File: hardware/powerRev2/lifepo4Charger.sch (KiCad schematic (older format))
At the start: 18 parts

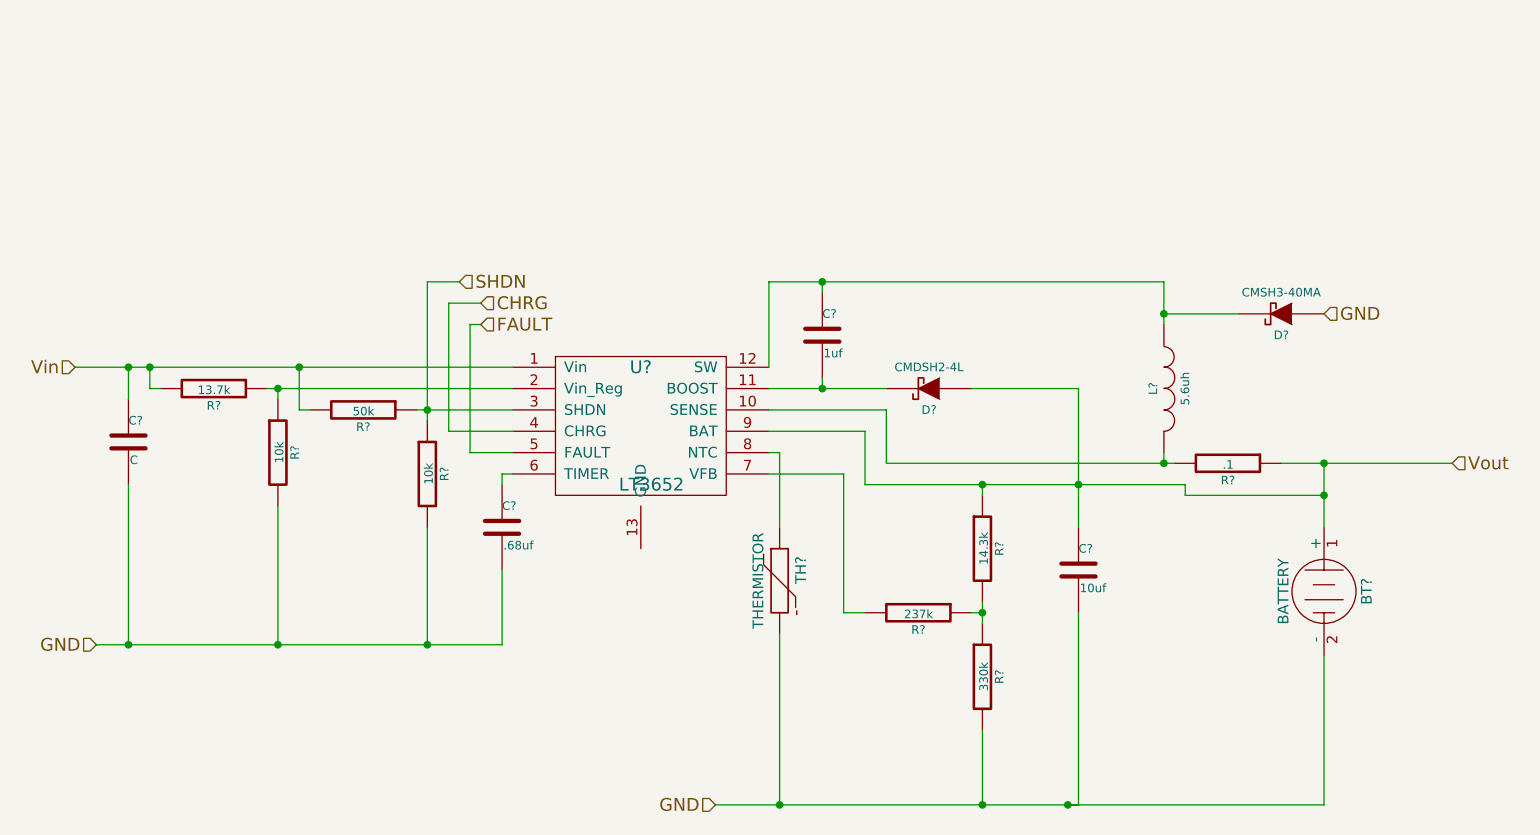
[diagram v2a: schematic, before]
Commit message: More work on the power supply
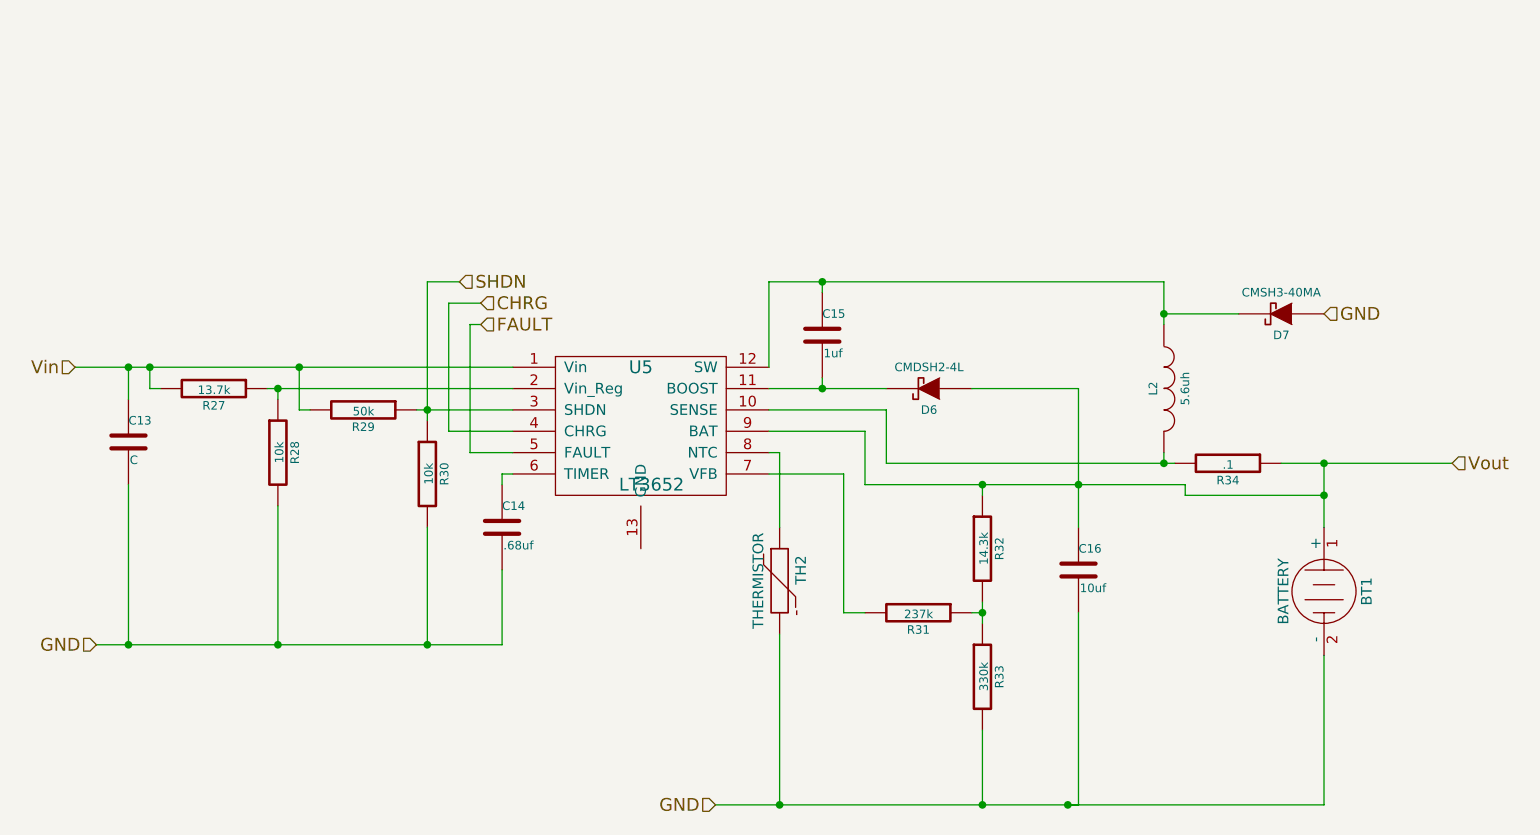
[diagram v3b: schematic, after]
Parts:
- gave numbers to parts that had none: 18
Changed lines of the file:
@@
 LIBS:KL03-QFN24
 LIBS:ncp508
+LIBS:hardwareRev1-cache
 LIBS:powerRev2-cache
 EELAYER 25 0
@@
 $EndDescr
 $Comp
-L LT3652 U?
+L LT3652 U5
 U 1 1 56114C94
 P 5850 3100
-F 0 "U?" H 5850 3400 60  0000 C CNN
+F 0 "U5" H 5850 3400 60  0000 C CNN
 F 1 "LT3652" H 5900 2850 60  0000 C CNN
 F 2 "" H 5850 2400 60  0000 C CNN
@@
 $EndComp
 $Comp
-L C C?
+L C C13
 U 1 1 56114CEB
 P 3450 3150
-F 0 "C?" H 3450 3250 40  0000 L CNN
+F 0 "C13" H 3450 3250 40  0000 L CNN
 F 1 "C" H 3456 3065 40  0000 L CNN
 F 2 "" H 3488 3000 30  0000 C CNN
@@
 $EndComp
 $Comp
-L R R?
+L R R27
 U 1 1 56114D05
 P 3850 2900
-F 0 "R?" V 3930 2900 40  0000 C CNN
+F 0 "R27" V 3930 2900 40  0000 C CNN
 F 1 "13.7k" V 3857 2901 40  0000 C CNN
 F 2 "" V 3780 2900 30  0000 C CNN
@@
 $EndComp
 $Comp
-L R R?
+L R R28
 U 1 1 56114DC8
 P 4150 3200
-F 0 "R?" V 4230 3200 40  0000 C CNN
+F 0 "R28" V 4230 3200 40  0000 C CNN
 F 1 "10k" V 4157 3201 40  0000 C CNN
 F 2 "" V 4080 3200 30  0000 C CNN
@@
 Vin
 $Comp
-L C C?
+L C C15
 U 1 1 56114F88
 P 6700 2650
-F 0 "C?" H 6700 2750 40  0000 L CNN
+F 0 "C15" H 6700 2750 40  0000 L CNN
 F 1 "1uf" H 6706 2565 40  0000 L CNN
 F 2 "" H 6738 2500 30  0000 C CNN
@@
 $EndComp
 $Comp
-L INDUCTOR L?
+L INDUCTOR L2
 U 1 1 56114FE2
 P 8300 2900
-F 0 "L?" V 8250 2900 40  0000 C CNN
+F 0 "L2" V 8250 2900 40  0000 C CNN
 F 1 "5.6uh" V 8400 2900 40  0000 C CNN
 F 2 "" H 8300 2900 60  0000 C CNN
@@
 $EndComp
 $Comp
-L DIODESCH D?
+L DIODESCH D7
 U 1 1 56115039
 P 8850 2550
-F 0 "D?" H 8850 2650 40  0000 C CNN
+F 0 "D7" H 8850 2650 40  0000 C CNN
 F 1 "CMSH3-40MA" H 8850 2450 40  0000 C CNN
 F 2 "" H 8850 2550 60  0000 C CNN
@@
 GND
 $Comp
-L C C?
+L C C16
 U 1 1 561153DF
 P 7900 3750
-F 0 "C?" H 7900 3850 40  0000 L CNN
+F 0 "C16" H 7900 3850 40  0000 L CNN
 F 1 "10uf" H 7906 3665 40  0000 L CNN
 F 2 "" H 7938 3600 30  0000 C CNN
@@
 $EndComp
 $Comp
-L BATTERY BT?
+L BATTERY BT1
 U 1 1 5611543C
 P 9050 3850
-F 0 "BT?" H 9050 4050 50  0000 C CNN
+F 0 "BT1" H 9050 4050 50  0000 C CNN
 F 1 "BATTERY" H 9050 3660 50  0000 C CNN
 F 2 "" H 9050 3850 60  0000 C CNN
@@
 	7900 2900 7900 3550
 $Comp
-L R R?
+L R R34
 U 1 1 56115725
 P 8600 3250
-F 0 "R?" V 8680 3250 40  0000 C CNN
+F 0 "R34" V 8680 3250 40  0000 C CNN
 F 1 ".1" V 8607 3251 40  0000 C CNN
 F 2 "" V 8530 3250 30  0000 C CNN
@@
 Connection ~ 9050 3400
 $Comp
-L THERMISTOR TH?
+L THERMISTOR TH2
 U 1 1 56115896
 P 6500 3800
-F 0 "TH?" V 6600 3850 50  0000 C CNN
+F 0 "TH2" V 6600 3850 50  0000 C CNN
 F 1 "THERMISTOR" V 6400 3800 50  0000 C CNN
 F 2 "" H 6500 3800 60  0000 C CNN
@@
 $EndComp
 $Comp
-L R R?
+L R R31
 U 1 1 561158DE
 P 7150 3950
-F 0 "R?" V 7230 3950 40  0000 C CNN
+F 0 "R31" V 7230 3950 40  0000 C CNN
 F 1 "237k" V 7157 3951 40  0000 C CNN
 F 2 "" V 7080 3950 30  0000 C CNN
@@
 $EndComp
 $Comp
-L R R?
+L R R32
 U 1 1 56115929
 P 7450 3650
-F 0 "R?" V 7530 3650 40  0000 C CNN
+F 0 "R32" V 7530 3650 40  0000 C CNN
 F 1 "14.3k" V 7457 3651 40  0000 C CNN
 F 2 "" V 7380 3650 30  0000 C CNN
@@
 $EndComp
 $Comp
-L R R?
+L R R33
 U 1 1 561159A8
 P 7450 4250
-F 0 "R?" V 7530 4250 40  0000 C CNN
+F 0 "R33" V 7530 4250 40  0000 C CNN
 F 1 "330k" V 7457 4251 40  0000 C CNN
 F 2 "" V 7380 4250 30  0000 C CNN
@@
 Connection ~ 4150 2900
 $Comp
-L R R?
+L R R29
 U 1 1 561165A5
 P 4550 3000
-F 0 "R?" V 4630 3000 40  0000 C CNN
+F 0 "R29" V 4630 3000 40  0000 C CNN
 F 1 "50k" V 4557 3001 40  0000 C CNN
 F 2 "" V 4480 3000 30  0000 C CNN
@@
 $EndComp
 $Comp
-L R R?
+L R R30
 U 1 1 561165FC
 P 4850 3300
-F 0 "R?" V 4930 3300 40  0000 C CNN
+F 0 "R30" V 4930 3300 40  0000 C CNN
 F 1 "10k" V 4857 3301 40  0000 C CNN
 F 2 "" V 4780 3300 30  0000 C CNN
@@
 FAULT
 $Comp
-L C C?
+L C C14
 U 1 1 56116AAD
 P 5200 3550
-F 0 "C?" H 5200 3650 40  0000 L CNN
+F 0 "C14" H 5200 3650 40  0000 L CNN
 F 1 ".68uf" H 5206 3465 40  0000 L CNN
 F 2 "" H 5238 3400 30  0000 C CNN
@@
 	5200 3300 5250 3300
 $Comp
-L DIODESCH D?
+L DIODESCH D6
 U 1 1 56116E89
 P 7200 2900
-F 0 "D?" H 7200 3000 40  0000 C CNN
+F 0 "D6" H 7200 3000 40  0000 C CNN
 F 1 "CMDSH2-4L" H 7200 2800 40  0000 C CNN
 F 2 "" H 7200 2900 60  0000 C CNN

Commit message: Started the new power board PCB. Made it pretty far.
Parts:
- C13: value C -> 10uf; footprint (none) -> Capacitors_SMD:C_0805
- C14: footprint (none) -> Capacitors_SMD:C_0402; Manufacturer PN (none) -> CL21F684ZAFNNNE
- C15: footprint (none) -> Capacitors_SMD:C_0402
- C16: footprint (none) -> Capacitors_SMD:C_0805
- D6: footprint (none) -> Diodes_SMD:SOD-323
- D7: footprint (none) -> Diodes_SMD:Diode-SMA_Standard
- L2: footprint (none) -> ASPI-6045S-5R6M-T:ASPI-6045S-5R6M-T; Manufacturer PN (none) -> ASPI-6045S-5R6M-T
- R27, R28, R29, R30, R31, R32, R33: footprint (none) -> Resistors_SMD:R_0402
- R34: footprint (none) -> Resistors_SMD:R_0805
- TH2: footprint (none) -> Pin_Headers:Pin_Header_Straight_1x02
- U6: renamed from U5; footprint (none) -> Housings_DFN_QFN:DFN-12-1EP_3x3mm_Pitch0.45mm
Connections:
- net GND: now also U6.13 (GND)
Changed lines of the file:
@@
 LIBS:ncp508
 LIBS:hardwareRev1-cache
+LIBS:Tag-Connect
+LIBS:mpcie
+LIBS:RF-Head2
+LIBS:ritli-rfhead
 LIBS:powerRev2-cache
 EELAYER 25 0
@@
 $EndDescr
 $Comp
-L LT3652 U5
+L LT3652 U6
 U 1 1 56114C94
 P 5850 3100
-F 0 "U5" H 5850 3400 60  0000 C CNN
+F 0 "U6" H 5850 3400 60  0000 C CNN
 F 1 "LT3652" H 5900 2850 60  0000 C CNN
-F 2 "" H 5850 2400 60  0000 C CNN
+F 2 "Housings_DFN_QFN:DFN-12-1EP_3x3mm_Pitch0.45mm" H 5850 2400 60  0001 C CNN
 F 3 "" H 5850 2400 60  0000 C CNN
 	1    5850 3100
@@
 P 3450 3150
 F 0 "C13" H 3450 3250 40  0000 L CNN
-F 1 "C" H 3456 3065 40  0000 L CNN
-F 2 "" H 3488 3000 30  0000 C CNN
+F 1 "10uf" H 3456 3065 40  0000 L CNN
+F 2 "Capacitors_SMD:C_0805" H 3488 3000 30  0001 C CNN
 F 3 "" H 3450 3150 60  0000 C CNN
 	1    3450 3150
@@
 F 0 "R27" V 3930 2900 40  0000 C CNN
 F 1 "13.7k" V 3857 2901 40  0000 C CNN
-F 2 "" V 3780 2900 30  0000 C CNN
+F 2 "Resistors_SMD:R_0402" V 3780 2900 30  0001 C CNN
 F 3 "" H 3850 2900 30  0000 C CNN
 	1    3850 2900
@@
 F 0 "R28" V 4230 3200 40  0000 C CNN
 F 1 "10k" V 4157 3201 40  0000 C CNN
-F 2 "" V 4080 3200 30  0000 C CNN
+F 2 "Resistors_SMD:R_0402" V 4080 3200 30  0001 C CNN
 F 3 "" H 4150 3200 30  0000 C CNN
 	1    4150 3200
@@
 F 0 "C15" H 6700 2750 40  0000 L CNN
 F 1 "1uf" H 6706 2565 40  0000 L CNN
-F 2 "" H 6738 2500 30  0000 C CNN
+F 2 "Capacitors_SMD:C_0402" H 6738 2500 30  0001 C CNN
 F 3 "" H 6700 2650 60  0000 C CNN
 	1    6700 2650
@@
 F 0 "L2" V 8250 2900 40  0000 C CNN
 F 1 "5.6uh" V 8400 2900 40  0000 C CNN
-F 2 "" H 8300 2900 60  0000 C CNN
+F 2 "ASPI-6045S-5R6M-T:ASPI-6045S-5R6M-T" H 8300 2900 60  0001 C CNN
 F 3 "" H 8300 2900 60  0000 C CNN
+F 4 "ASPI-6045S-5R6M-T" H 8300 2900 60  0001 C CNN "Manufacturer PN"
 	1    8300 2900
 	1    0    0    -1
@@
 F 0 "D7" H 8850 2650 40  0000 C CNN
 F 1 "CMSH3-40MA" H 8850 2450 40  0000 C CNN
-F 2 "" H 8850 2550 60  0000 C CNN
+F 2 "Diodes_SMD:Diode-SMA_Standard" H 8850 2550 60  0001 C CNN
 F 3 "" H 8850 2550 60  0000 C CNN
 	1    8850 2550
@@
 F 0 "C16" H 7900 3850 40  0000 L CNN
 F 1 "10uf" H 7906 3665 40  0000 L CNN
-F 2 "" H 7938 3600 30  0000 C CNN
+F 2 "Capacitors_SMD:C_0805" H 7938 3600 30  0001 C CNN
 F 3 "" H 7900 3750 60  0000 C CNN
 	1    7900 3750
@@
 F 0 "BT1" H 9050 4050 50  0000 C CNN
 F 1 "BATTERY" H 9050 3660 50  0000 C CNN
-F 2 "" H 9050 3850 60  0000 C CNN
+F 2 "" H 9050 3850 60  0001 C CNN
 F 3 "" H 9050 3850 60  0000 C CNN
 	1    9050 3850
@@
 F 0 "R34" V 8680 3250 40  0000 C CNN
 F 1 ".1" V 8607 3251 40  0000 C CNN
-F 2 "" V 8530 3250 30  0000 C CNN
+F 2 "Resistors_SMD:R_0805" V 8530 3250 30  0001 C CNN
 F 3 "" H 8600 3250 30  0000 C CNN
 	1    8600 3250
@@
 F 0 "TH2" V 6600 3850 50  0000 C CNN
 F 1 "THERMISTOR" V 6400 3800 50  0000 C CNN
-F 2 "" H 6500 3800 60  0000 C CNN
+F 2 "Pin_Headers:Pin_Header_Straight_1x02" H 6500 3800 60  0001 C CNN
 F 3 "" H 6500 3800 60  0000 C CNN
 	1    6500 3800
@@
 F 0 "R31" V 7230 3950 40  0000 C CNN
 F 1 "237k" V 7157 3951 40  0000 C CNN
-F 2 "" V 7080 3950 30  0000 C CNN
+F 2 "Resistors_SMD:R_0402" V 7080 3950 30  0001 C CNN
 F 3 "" H 7150 3950 30  0000 C CNN
 	1    7150 3950
@@
 F 0 "R32" V 7530 3650 40  0000 C CNN
 F 1 "14.3k" V 7457 3651 40  0000 C CNN
-F 2 "" V 7380 3650 30  0000 C CNN
+F 2 "Resistors_SMD:R_0402" V 7380 3650 30  0001 C CNN
 F 3 "" H 7450 3650 30  0000 C CNN
 	1    7450 3650
@@
 F 0 "R33" V 7530 4250 40  0000 C CNN
 F 1 "330k" V 7457 4251 40  0000 C CNN
-F 2 "" V 7380 4250 30  0000 C CNN
+F 2 "Resistors_SMD:R_0402" V 7380 4250 30  0001 C CNN
 F 3 "" H 7450 4250 30  0000 C CNN
 	1    7450 4250
@@
 F 0 "R29" V 4630 3000 40  0000 C CNN
 F 1 "50k" V 4557 3001 40  0000 C CNN
-F 2 "" V 4480 3000 30  0000 C CNN
+F 2 "Resistors_SMD:R_0402" V 4480 3000 30  0001 C CNN
 F 3 "" H 4550 3000 30  0000 C CNN
 	1    4550 3000
@@
 F 0 "R30" V 4930 3300 40  0000 C CNN
 F 1 "10k" V 4857 3301 40  0000 C CNN
-F 2 "" V 4780 3300 30  0000 C CNN
+F 2 "Resistors_SMD:R_0402" V 4780 3300 30  0001 C CNN
 F 3 "" H 4850 3300 30  0000 C CNN
 	1    4850 3300
@@
 F 0 "C14" H 5200 3650 40  0000 L CNN
 F 1 ".68uf" H 5206 3465 40  0000 L CNN
-F 2 "" H 5238 3400 30  0000 C CNN
+F 2 "Capacitors_SMD:C_0402" H 5238 3400 30  0001 C CNN
 F 3 "" H 5200 3550 60  0000 C CNN
+F 4 "CL21F684ZAFNNNE" H 5200 3550 60  0001 C CNN "Manufacturer PN"
 	1    5200 3550
 	1    0    0    -1
@@
 F 0 "D6" H 7200 3000 40  0000 C CNN
 F 1 "CMDSH2-4L" H 7200 2800 40  0000 C CNN
-F 2 "" H 7200 2900 60  0000 C CNN
+F 2 "Diodes_SMD:SOD-323" H 7200 2900 60  0001 C CNN
 F 3 "" H 7200 2900 60  0000 C CNN
 	1    7200 2900
@@
 GND
 Wire Wire Line
-	3300 4100 5200 4100
+	3300 4100 5850 4100
 Wire Wire Line
 	5200 4100 5200 3750
@@
 	3450 3350 3450 4100
 Connection ~ 3450 4100
+Wire Wire Line
+	5850 4100 5850 3650
+Connection ~ 5200 4100
 $EndSCHEMATC

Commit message: Finished the new power board.
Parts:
- added BT2: BATTERY, Pin_Headers:Pin_Header_Straight_1x02, symbol BATTERY
- added P11: HOLE_1, Mounting_Holes:MountingHole_2-5mm, symbol CONN_1
- added P12: HOLE_2, Mounting_Holes:MountingHole_2-5mm, symbol CONN_1
- added P13: HOLE_3, Mounting_Holes:MountingHole_2-5mm, symbol CONN_1
- added P14: HOLE_4, Mounting_Holes:MountingHole_2-5mm, symbol CONN_1
- BT1: footprint (none) -> hardwareRev1:lifepo4-1004045-3C-folded
- R29: value 50k -> 49.9K
- TH2: Manufacturer PN (none) -> NTCLE100E3103JB0
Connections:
- net GND: now also BT2.2 (-)
- net Vout: now also BT2.1 (+)
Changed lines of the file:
@@
 EESchema Schematic File Version 2
+LIBS:powerRev2-rescue
 LIBS:power
 LIBS:device
@@
 LIBS:RF-Head2
 LIBS:ritli-rfhead
+LIBS:mos_n_numbered
+LIBS:npn-numbered
 LIBS:powerRev2-cache
 EELAYER 25 0
@@
 F 0 "BT1" H 9050 4050 50  0000 C CNN
 F 1 "BATTERY" H 9050 3660 50  0000 C CNN
-F 2 "" H 9050 3850 60  0001 C CNN
+F 2 "hardwareRev1:lifepo4-1004045-3C-folded" H 9050 3850 60  0001 C CNN
 F 3 "" H 9050 3850 60  0000 C CNN
 	1    9050 3850
@@
 F 2 "Pin_Headers:Pin_Header_Straight_1x02" H 6500 3800 60  0001 C CNN
 F 3 "" H 6500 3800 60  0000 C CNN
+F 4 "NTCLE100E3103JB0" H 6500 3800 60  0001 C CNN "Manufacturer PN"
 	1    6500 3800
 	1    0    0    -1
@@
 P 4550 3000
 F 0 "R29" V 4630 3000 40  0000 C CNN
-F 1 "50k" V 4557 3001 40  0000 C CNN
+F 1 "49.9K" V 4557 3001 40  0000 C CNN
 F 2 "Resistors_SMD:R_0402" V 4480 3000 30  0001 C CNN
 F 3 "" H 4550 3000 30  0000 C CNN
@@
 	5850 4100 5850 3650
 Connection ~ 5200 4100
+$Comp
+L BATTERY BT2
+U 1 1 5632D9D1
+P 9550 3850
+F 0 "BT2" H 9550 4050 50  0000 C CNN
+F 1 "BATTERY" H 9550 3660 50  0000 C CNN
+F 2 "Pin_Headers:Pin_Header_Straight_1x02" H 9550 3850 60  0001 C CNN
+F 3 "" H 9550 3850 60  0000 C CNN
+	1    9550 3850
+	0    1    1    0
+$EndComp
+Wire Wire Line
+	9550 3550 9550 3450
+Wire Wire Line
+	9550 3450 9050 3450
+Connection ~ 9050 3450
+Wire Wire Line
+	9550 4150 9550 4250
+Wire Wire Line
+	9550 4250 9050 4250
+Connection ~ 9050 4250
+$Comp
+L CONN_1 P11
+U 1 1 5640F74A
+P 7850 1200
+F 0 "P11" H 7930 1200 40  0000 L CNN
+F 1 "HOLE_1" H 7850 1255 30  0001 C CNN
+F 2 "Mounting_Holes:MountingHole_2-5mm" H 7850 1200 60  0001 C CNN
+F 3 "" H 7850 1200 60  0000 C CNN
+	1    7850 1200
+	1    0    0    -1
+$EndComp
+$Comp
+L CONN_1 P12
+U 1 1 5640F8B5
+P 7850 1350
+F 0 "P12" H 7930 1350 40  0000 L CNN
+F 1 "HOLE_2" H 7850 1405 30  0001 C CNN
+F 2 "Mounting_Holes:MountingHole_2-5mm" H 7850 1350 60  0001 C CNN
+F 3 "" H 7850 1350 60  0000 C CNN
+	1    7850 1350
+	1    0    0    -1
+$EndComp
+$Comp
+L CONN_1 P13
+U 1 1 5640F8FF
+P 7850 1500
+F 0 "P13" H 7930 1500 40  0000 L CNN
+F 1 "HOLE_3" H 7850 1555 30  0001 C CNN
+F 2 "Mounting_Holes:MountingHole_2-5mm" H 7850 1500 60  0001 C CNN
+F 3 "" H 7850 1500 60  0000 C CNN
+	1    7850 1500
+	1    0    0    -1
+$EndComp
+$Comp
+L CONN_1 P14
+U 1 1 5640F93F
+P 7850 1650
+F 0 "P14" H 7930 1650 40  0000 L CNN
+F 1 "HOLE_4" H 7850 1705 30  0001 C CNN
+F 2 "Mounting_Holes:MountingHole_2-5mm" H 7850 1650 60  0001 C CNN
+F 3 "" H 7850 1650 60  0000 C CNN
+	1    7850 1650
+	1    0    0    -1
+$EndComp
 $EndSCHEMATC
